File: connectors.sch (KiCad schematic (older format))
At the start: 5 parts, among them J1 ARJ-169, M1 ET60S-02-24-02-X-VP-GP, M2 ET60S-02-24-02-X-VP-GP, M3 ET60S-02-24-02-X-VP-GP, M4 ET60S-02-24-02-X-VP-GP

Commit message: layout stuff
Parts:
- added C17, C18: C_Small, Capacitor_SMD:C_0603_1608Metric, symbol Device:C_Small
- added J2: USB_B, Connector_USB:USB_B_OST_USB-B1HSxx_Horizontal, symbol Connector:USB_B
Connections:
- net labels added: +3.3V, +5V, +BATT, GND, RD_N, RD_P, TD_N, TD_P, USB_JTAG_N, USB_JTAG_P, USB_OTG_N, USB_OTG_P
- wire segments 0 -> 195

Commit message: usb hub and sdram selected.
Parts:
- removed J2: USB_B, Connector_USB:USB_B_OST_USB-B1HSxx_Horizontal, symbol Connector:USB_B
- added J2: USB_B_Mini, Connector_USB:USB_Mini-B_Lumberg_2486_01_Horizontal, symbol Connector:USB_B_Mini
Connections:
- net labels added: JTAG_TCK, JTAG_TDI, JTAG_TDO, JTAG_TMS, ~JTAG_TRST
- net labels removed: USB_JTAG_N, USB_JTAG_P
- wire segments 195 -> 200
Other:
- moved on the sheet: M3A, M4A
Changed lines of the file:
@@
 $Descr A4 11693 8268
 encoding utf-8
-Sheet 4 4
+Sheet 3 5
 Title ""
-Date ""
+Date "2019-03-16"
 Rev ""
-Comp ""
+Comp "Exodus"
 Comment1 ""
 Comment2 ""
@@
 L ET60S-02-24-02-X-VP-GP:ET60S-02-24-02-X-VP-GP M?
 U 1 1 5C812DCB
-P 9150 1000
+P 9900 900
 AR Path="/5C812DCB" Ref="M?"  Part="1"
 AR Path="/5C8128A2/5C812DCB" Ref="M3"  Part="1"
-F 0 "M3" H 9678 -108 45  0000 L CNN
-F 1 "ET60S-02-24-02-X-VP-GP" H 9678 -192 45  0000 L CNN
-F 2 "Exodus_Connectors:ET60S-02-24-02-X-VP-GP" H 9180 1150 20  0001 C CNN
-F 3 "" H 9150 1000 50  0001 C CNN
-	1    9150 1000
+F 0 "M3" H 10428 -208 45  0000 L CNN
+F 1 "ET60S-02-24-02-X-VP-GP" H 10428 -292 45  0000 L CNN
+F 2 "Exodus_Connectors:ET60S-02-24-02-X-VP-GP" H 9930 1050 20  0001 C CNN
+F 3 "" H 9900 900 50  0001 C CNN
+	1    9900 900
 	1    0    0    -1
 $EndComp
@@
 L ET60S-02-24-02-X-VP-GP:ET60S-02-24-02-X-VP-GP M?
 U 1 1 5C812DE0
-P 9200 3700
+P 9900 3900
 AR Path="/5C812DE0" Ref="M?"  Part="1"
 AR Path="/5C8128A2/5C812DE0" Ref="M4"  Part="1"
-F 0 "M4" H 9728 2592 45  0000 L CNN
-F 1 "ET60S-02-24-02-X-VP-GP" H 9728 2508 45  0000 L CNN
-F 2 "Exodus_Connectors:ET60S-02-24-02-X-VP-GP" H 9230 3850 20  0001 C CNN
-F 3 "" H 9200 3700 50  0001 C CNN
-	1    9200 3700
+F 0 "M4" H 10428 2792 45  0000 L CNN
+F 1 "ET60S-02-24-02-X-VP-GP" H 10428 2708 45  0000 L CNN
+F 2 "Exodus_Connectors:ET60S-02-24-02-X-VP-GP" H 9930 4050 20  0001 C CNN
+F 3 "" H 9900 3900 50  0001 C CNN
+	1    9900 3900
 	1    0    0    -1
 $EndComp
@@
 	1    0    0    -1
 $EndComp
-$Comp
-L Connector:USB_B J2
-U 1 1 5C8C92DA
-P 5000 4400
-F 0 "J2" H 5055 4867 50  0000 C CNN
-F 1 "USB_B" H 5055 4776 50  0000 C CNN
-F 2 "Connector_USB:USB_B_OST_USB-B1HSxx_Horizontal" H 5150 4350 50  0001 C CNN
-F 3 " ~" H 5150 4350 50  0001 C CNN
-	1    5000 4400
-	1    0    0    -1
-$EndComp
 Wire Wire Line
 	3550 4450 3650 4450
@@
 $EndComp
 Wire Wire Line
-	5300 3350 5650 3350
-Wire Wire Line
-	5300 3450 5650 3450
-Text HLabel 5650 3350 2    50   Input ~ 0
+	5050 5600 4700 5600
+Wire Wire Line
+	5050 5500 4700 5500
+Text HLabel 4700 5600 0    50   Input ~ 0
 USB_OTG_N
-Text HLabel 5650 3450 2    50   Input ~ 0
+Text HLabel 4700 5500 0    50   Input ~ 0
 USB_OTG_P
-Wire Wire Line
-	5300 4400 5600 4400
-Wire Wire Line
-	5300 4500 5600 4500
-Text HLabel 5600 4400 2    50   Input ~ 0
-USB_JTAG_P
-Text HLabel 5600 4500 2    50   Input ~ 0
-USB_JTAG_N
 $Comp
 L power:GND #PWR0144
@@
 L power:GND #PWR0145
 U 1 1 5C92F187
-P 5000 4900
-F 0 "#PWR0145" H 5000 4650 50  0001 C CNN
-F 1 "GND" H 5005 4727 50  0000 C CNN
-F 2 "" H 5000 4900 50  0001 C CNN
-F 3 "" H 5000 4900 50  0001 C CNN
-	1    5000 4900
-	1    0    0    -1
-$EndComp
-Wire Wire Line
-	4900 4800 5000 4800
-Wire Wire Line
-	5000 4800 5000 4900
-Connection ~ 5000 4800
+P 4650 4900
+F 0 "#PWR0145" H 4650 4650 50  0001 C CNN
+F 1 "GND" H 4655 4727 50  0000 C CNN
+F 2 "" H 4650 4900 50  0001 C CNN
+F 3 "" H 4650 4900 50  0001 C CNN
+	1    4650 4900
+	1    0    0    -1
+$EndComp
+Wire Wire Line
+	4650 4800 4650 4900
 Wire Wire Line
 	5400 1650 5700 1650
@@
 Wire Wire Line
 	6100 2000 6100 2050
+$Comp
+L Connector:USB_B_Mini J2
+U 1 1 5C8E55A5
+P 4650 4400
+F 0 "J2" H 4705 4867 50  0000 C CNN
+F 1 "USB_B_Mini" H 4705 4776 50  0000 C CNN
+F 2 "Connector_USB:USB_Mini-B_Lumberg_2486_01_Horizontal" H 4800 4350 50  0001 C CNN
+F 3 "~" H 4800 4350 50  0001 C CNN
+	1    4650 4400
+	1    0    0    -1
+$EndComp
+Wire Wire Line
+	4550 4800 4650 4800
+Connection ~ 4650 4800
+$Sheet
+S 5050 5400 1150 1550
+U 5C922FFC
+F0 "sheet5C922FED" 50
+F1 "usb_hub.sch" 50
+F2 "upstream_usb_p" I L 5050 5500 50
+F3 "upstream_usb_n" I L 5050 5600 50
+F4 "~RESET" I L 5050 5750 50
+F5 "D5_P" I R 6200 5650 50
+F6 "D5_N" I R 6200 5750 50
+F7 "D4_P" I R 6200 5950 50
+F8 "D4_N" I R 6200 6050 50
+F9 "D3_P" I R 6200 6200 50
+F10 "D3_N" I R 6200 6300 50
+F11 "D2_P" I R 6200 6450 50
+F12 "D2_N" I R 6200 6550 50
+F13 "D1_P" I R 6200 6700 50
+F14 "D1_N" I R 6200 6800 50
+$EndSheet
+$Sheet
+S 5200 4250 900  800
+U 5C96EC24
+F0 "sheet5C96EC1B" 50
+F1 "ft232h.sch" 50
+F2 "D-" I L 5200 4500 50
+F3 "D+" I L 5200 4400 50
+F4 "ADBUS0" I R 6100 4350 50
+F5 "ADBUS1" I R 6100 4450 50
+F6 "ADBUS2" I R 6100 4550 50
+F7 "ADBUS3" I R 6100 4650 50
+F8 "ADBUS4" I R 6100 4750 50
+$EndSheet
+Wire Wire Line
+	6100 4350 6450 4350
+Wire Wire Line
+	6100 4450 6450 4450
+Wire Wire Line
+	6100 4550 6450 4550
+Wire Wire Line
+	6100 4650 6450 4650
+Text Label 6450 4350 0    50   ~ 0
+JTAG_TCK
+Text Label 6450 4450 0    50   ~ 0
+JTAG_TDI
+Text Label 6450 4550 0    50   ~ 0
+JTAG_TDO
+Text Label 6450 4650 0    50   ~ 0
+JTAG_TMS
+Wire Wire Line
+	6100 4750 6450 4750
+Text Label 6450 4750 0    50   ~ 0
+~JTAG_TRST
+Wire Wire Line
+	4950 4400 5200 4400
+Wire Wire Line
+	4950 4500 5200 4500
 $EndSCHEMATC

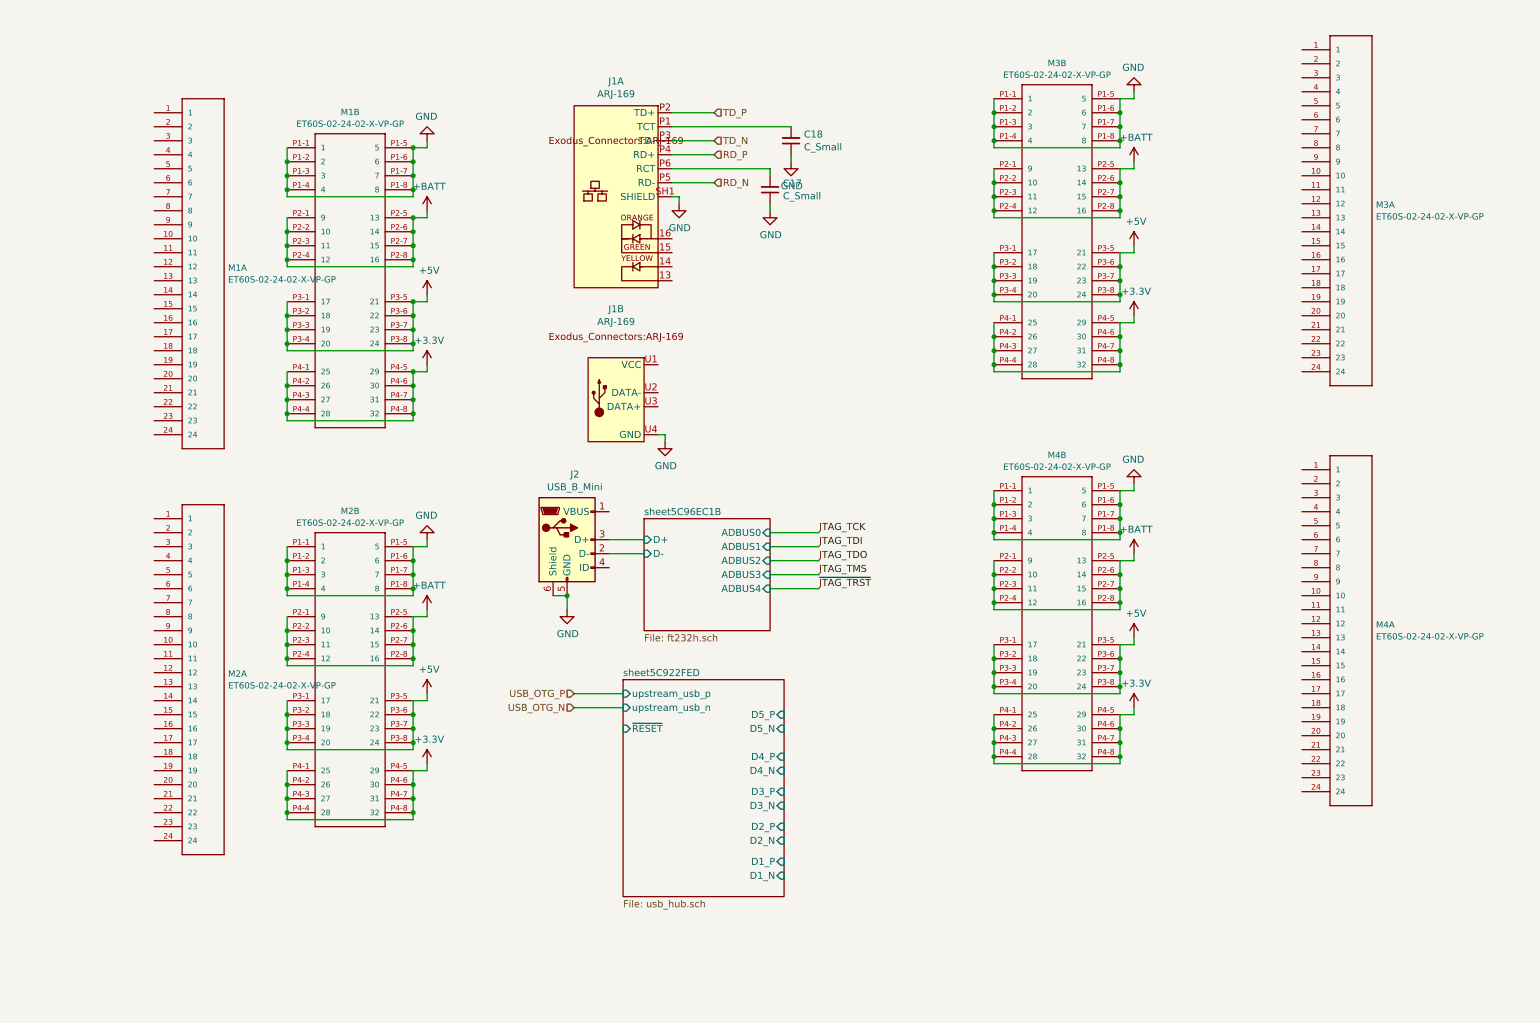
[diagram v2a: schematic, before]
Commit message: schematics for expansion slots and memory
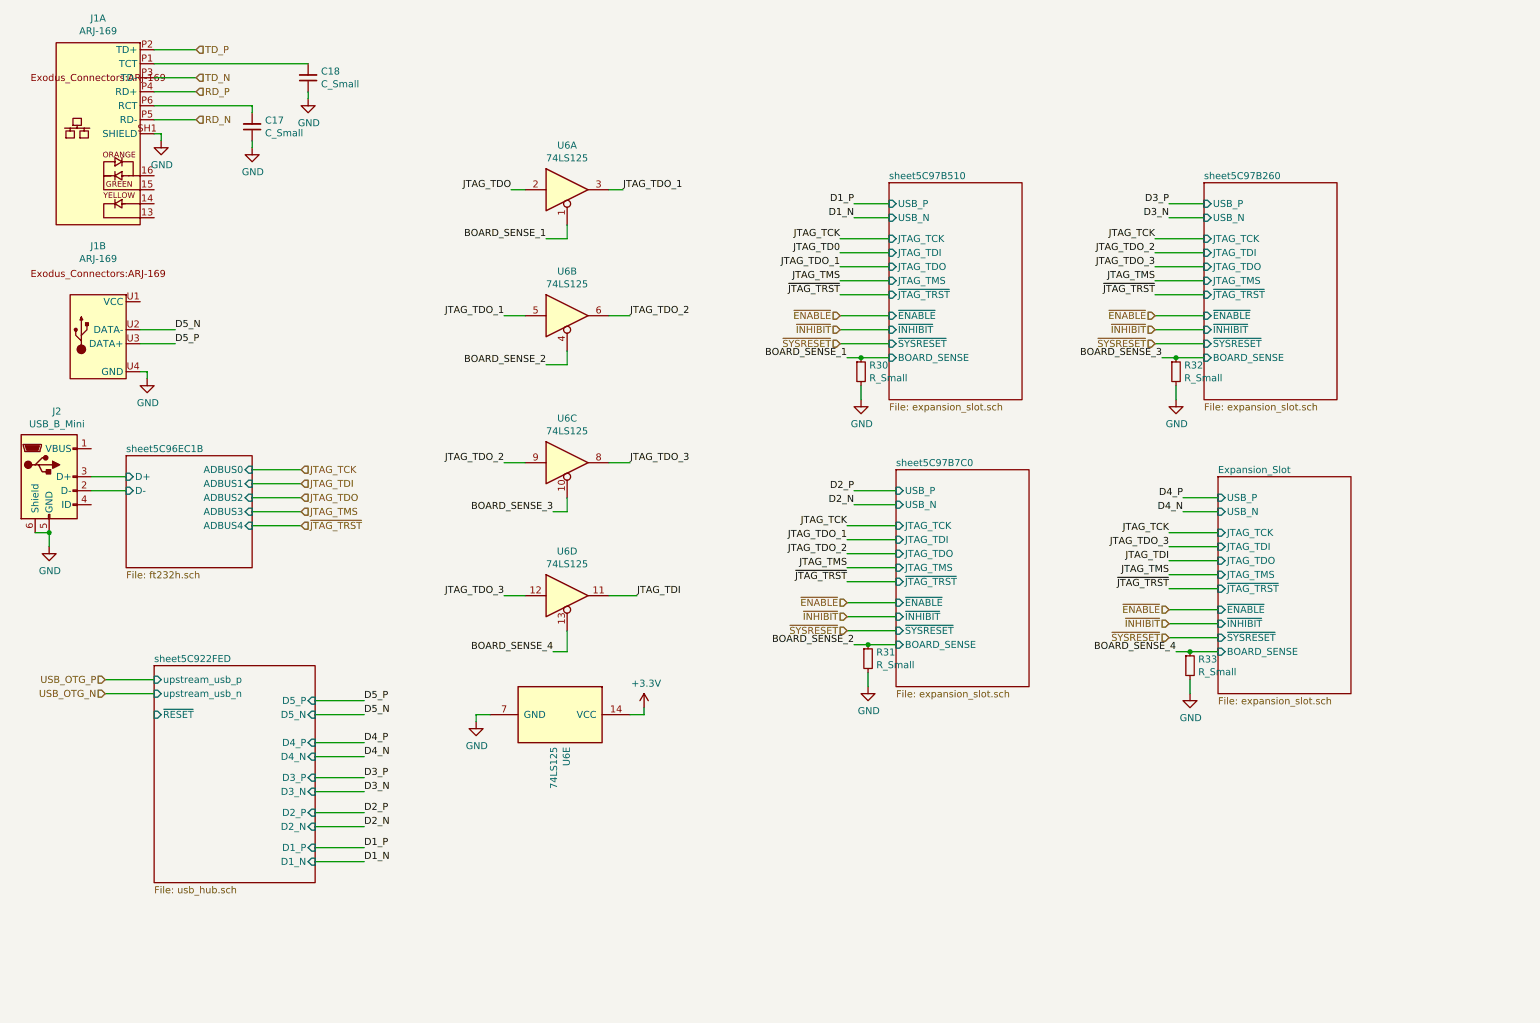
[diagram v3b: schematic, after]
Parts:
- removed M1, M2, M3, M4: ET60S-02-24-02-X-VP-GP, Exodus_Connectors:ET60S-02-24-02-X-VP-GP, symbol ET60S-02-24-02-X-VP-GP:ET60S-02-24-02-X-VP-GP
- added R30, R31, R32, R33: R_Small, Resistor_SMD:R_0603_1608Metric, symbol Device:R_Small
- added U6: 74LS125, Package_SO:SOIC-14_3.9x8.7mm_P1.27mm, symbol 74xx:74LS125
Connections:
- net +3V3: now also U6.14 (VCC)
- net GND: now also R30.2, R31.2, R32.2, R33.2, U6.7 (GND)
- net JTAG_TDI: now also U6.11
- net JTAG_TDO: now also U6.2
- net D5_N: now reaches J1.U2 (DATA-)
- net D5_P: now reaches J1.U3 (DATA+)
- new net BOARD_SENSE_1: R30.1, U6.1
- new net BOARD_SENSE_2: R31.1, U6.4
- new net BOARD_SENSE_3: R32.1, U6.10
- new net BOARD_SENSE_4: R33.1, U6.13
- new net JTAG_TDO_1: U6.3, U6.5
- new net JTAG_TDO_2: U6.6, U6.9
- new net JTAG_TDO_3: U6.12, U6.8
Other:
- moved on the sheet: C17, C18, J1A, J1B, J2

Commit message: fixing up the jtag connections. Should be good now
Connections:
- net JTAG_TDI renamed JTAG_TDO_4
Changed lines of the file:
@@
 Wire Wire Line
 	6950 2450 6600 2450
-Text Label 6600 2350 2    50   ~ 0
-JTAG_TD0
 Text Label 6600 2450 2    50   ~ 0
 JTAG_TDO_1
@@
 	9300 4550 8950 4550
 Text Label 8950 4550 2    50   ~ 0
-JTAG_TDI
+JTAG_TDO_4
 $Comp
 L 74xx:74LS125 U6
@@
 	4950 4800 5150 4800
 Text Label 5150 4800 0    50   ~ 0
-JTAG_TDI
+JTAG_TDO_4
 Text Label 4200 4800 2    50   ~ 0
 JTAG_TDO_3
@@
 Wire Wire Line
 	4000 5650 4000 5700
+Text HLabel 2750 4100 2    50   Input ~ 0
+JTAG_TDI_MCU
+Text HLabel 6600 2350 0    50   Input ~ 0
+JTAG_TDO_MCU
+Text Label 2750 4000 0    50   ~ 0
+JTAG_TDO_4
 Text HLabel 2750 4300 2    50   Input ~ 0
 ~JTAG_TRST
 Text HLabel 2750 4200 2    50   Input ~ 0
 JTAG_TMS
-Text HLabel 2750 4100 2    50   Input ~ 0
-JTAG_TDO
-Text HLabel 2750 4000 2    50   Input ~ 0
-JTAG_TDI
 Text HLabel 2750 3900 2    50   Input ~ 0
 JTAG_TCK

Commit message: almost done with draft 1 of layout
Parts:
- removed R30, R31, R32, R33: R_Small, Resistor_SMD:R_0603_1608Metric, symbol Device:R_Small
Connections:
- net JTAG_TDO is gone; now on net JTAG_TDO_MCU: U6.2
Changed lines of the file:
@@
 	4950 2800 5100 2800
 Text Label 4250 1900 2    50   ~ 0
-JTAG_TDO
+JTAG_TDO_MCU
 Text Label 5050 1900 0    50   ~ 0
 JTAG_TDO_1
@@
 Wire Wire Line
 	4650 5200 4550 5200
-Wire Wire Line
-	6950 3100 6750 3100
-Wire Wire Line
-	7000 5150 6800 5150
-Wire Wire Line
-	9300 5200 9100 5200
-Wire Wire Line
-	9200 3100 9000 3100
 Text Label 9000 5200 2    50   ~ 0
 BOARD_SENSE_4
@@
 Text Label 1850 3000 0    50   ~ 0
 D5_P
-$Comp
-L Device:R_Small R30
-U 1 1 5CA39A7F
-P 6750 3200
-F 0 "R30" H 6809 3246 50  0000 L CNN
-F 1 "R_Small" H 6809 3155 50  0000 L CNN
-F 2 "Resistor_SMD:R_0603_1608Metric" H 6750 3200 50  0001 C CNN
-F 3 "~" H 6750 3200 50  0001 C CNN
-	1    6750 3200
-	1    0    0    -1
-$EndComp
-Connection ~ 6750 3100
-Wire Wire Line
-	6750 3100 6650 3100
-$Comp
-L Device:R_Small R31
-U 1 1 5CA39B69
-P 6800 5250
-F 0 "R31" H 6859 5296 50  0000 L CNN
-F 1 "R_Small" H 6859 5205 50  0000 L CNN
-F 2 "Resistor_SMD:R_0603_1608Metric" H 6800 5250 50  0001 C CNN
-F 3 "~" H 6800 5250 50  0001 C CNN
-	1    6800 5250
-	1    0    0    -1
-$EndComp
-Connection ~ 6800 5150
-Wire Wire Line
-	6800 5150 6700 5150
-$Comp
-L Device:R_Small R33
-U 1 1 5CA39BDF
-P 9100 5300
-F 0 "R33" H 9159 5346 50  0000 L CNN
-F 1 "R_Small" H 9159 5255 50  0000 L CNN
-F 2 "Resistor_SMD:R_0603_1608Metric" H 9100 5300 50  0001 C CNN
-F 3 "~" H 9100 5300 50  0001 C CNN
-	1    9100 5300
-	1    0    0    -1
-$EndComp
-Connection ~ 9100 5200
-Wire Wire Line
-	9100 5200 9000 5200
-$Comp
-L Device:R_Small R32
-U 1 1 5CA39C4D
-P 9000 3200
-F 0 "R32" H 9059 3246 50  0000 L CNN
-F 1 "R_Small" H 9059 3155 50  0000 L CNN
-F 2 "Resistor_SMD:R_0603_1608Metric" H 9000 3200 50  0001 C CNN
-F 3 "~" H 9000 3200 50  0001 C CNN
-	1    9000 3200
-	1    0    0    -1
-$EndComp
-Connection ~ 9000 3100
-Wire Wire Line
-	9000 3100 8900 3100
-Wire Wire Line
-	6750 3300 6750 3400
-Wire Wire Line
-	9000 3300 9000 3400
-Wire Wire Line
-	9100 5400 9100 5500
-Wire Wire Line
-	6800 5350 6800 5450
 Wire Wire Line
 	1700 1000 2800 1000
@@
 Text Label 6600 2650 2    50   ~ 0
 ~JTAG_TRST
-$Comp
-L power:GND #PWR0184
-U 1 1 5CA8CBD1
-P 9000 3400
-F 0 "#PWR0184" H 9000 3150 50  0001 C CNN
-F 1 "GND" H 9005 3227 50  0000 C CNN
-F 2 "" H 9000 3400 50  0001 C CNN
-F 3 "" H 9000 3400 50  0001 C CNN
-	1    9000 3400
-	1    0    0    -1
-$EndComp
-$Comp
-L power:GND #PWR0185
-U 1 1 5CA8CBFF
-P 6750 3400
-F 0 "#PWR0185" H 6750 3150 50  0001 C CNN
-F 1 "GND" H 6755 3227 50  0000 C CNN
-F 2 "" H 6750 3400 50  0001 C CNN
-F 3 "" H 6750 3400 50  0001 C CNN
-	1    6750 3400
-	1    0    0    -1
-$EndComp
-$Comp
-L power:GND #PWR0186
-U 1 1 5CA8CE72
-P 6800 5450
-F 0 "#PWR0186" H 6800 5200 50  0001 C CNN
-F 1 "GND" H 6805 5277 50  0000 C CNN
-F 2 "" H 6800 5450 50  0001 C CNN
-F 3 "" H 6800 5450 50  0001 C CNN
-	1    6800 5450
-	1    0    0    -1
-$EndComp
-$Comp
-L power:GND #PWR0187
-U 1 1 5CA8CE99
-P 9100 5500
-F 0 "#PWR0187" H 9100 5250 50  0001 C CNN
-F 1 "GND" H 9105 5327 50  0000 C CNN
-F 2 "" H 9100 5500 50  0001 C CNN
-F 3 "" H 9100 5500 50  0001 C CNN
-	1    9100 5500
-	1    0    0    -1
-$EndComp
 Wire Wire Line
 	9300 5100 8950 5100
@@
 Text HLabel 2750 3900 2    50   Input ~ 0
 JTAG_TCK
+Wire Wire Line
+	6700 5150 7000 5150
+Wire Wire Line
+	9000 5200 9300 5200
+Wire Wire Line
+	8900 3100 9200 3100
+Wire Wire Line
+	6650 3100 6950 3100
 $EndSCHEMATC

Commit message: layout done sans connector. It's pretty big. Likely going to need to tear some of this up.
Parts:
- added J4: Micro_SD_Card, Connector_Card:microSD_HC_Wuerth_693072010801, symbol Connector:Micro_SD_Card
- added R36: R_Small, Resistor_SMD:R_0603_1608Metric, symbol Device:R_Small
- added R?: R_Small, symbol Device:R_Small
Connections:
- net labels added: ETH_LED0, ETH_LED1, SPI_DAT2, SPI_DAT3, SPI_MISO, SPI_MOSI, SPI_SCLK, SPI_SS
- wire segments 100 -> 120
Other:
- moved on the sheet: U6A, U6B, U6C, U6D, U6E

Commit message: this is just a mess. but I think the schematic is basically right still.
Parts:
- removed C17, C18: C_Small, Capacitor_SMD:C_0603_1608Metric, symbol Device:C_Small
- removed J1: ARJ-169, Exodus_Connectors:ARJ-169, symbol Exodus_Connectors:ARJ-169
- removed J4: Micro_SD_Card, Connector_Card:microSD_HC_Wuerth_693072010801, symbol Connector:Micro_SD_Card
- removed R36: R_Small, Resistor_SMD:R_0603_1608Metric, symbol Device:R_Small
- removed R?: R_Small, symbol Device:R_Small
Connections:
- net labels removed: ETH_LED0, ETH_LED1, RD_N, RD_P, SPI_DAT2, SPI_DAT3, SPI_MISO, SPI_MOSI, SPI_SCLK, SPI_SS, TD_N, TD_P
- wire segments 120 -> 87
